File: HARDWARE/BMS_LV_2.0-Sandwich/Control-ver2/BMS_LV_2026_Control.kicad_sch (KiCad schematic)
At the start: 5 parts, among them J1 Conn_01x26

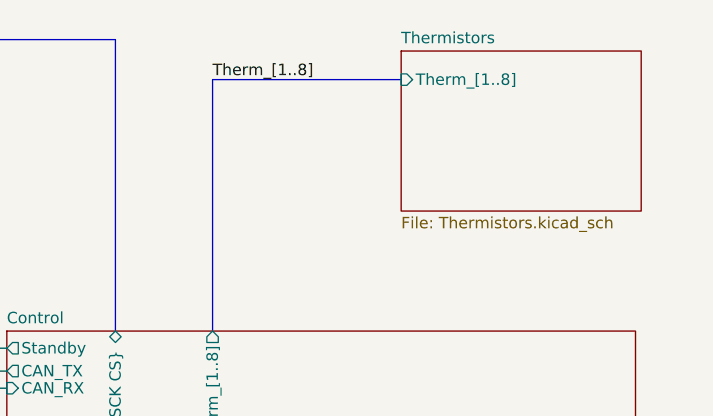
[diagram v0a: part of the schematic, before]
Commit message: Przesunięto złącze do thermistorów oraz programator aby nie bylo kolizji, przesunięto tez bezpieczniki
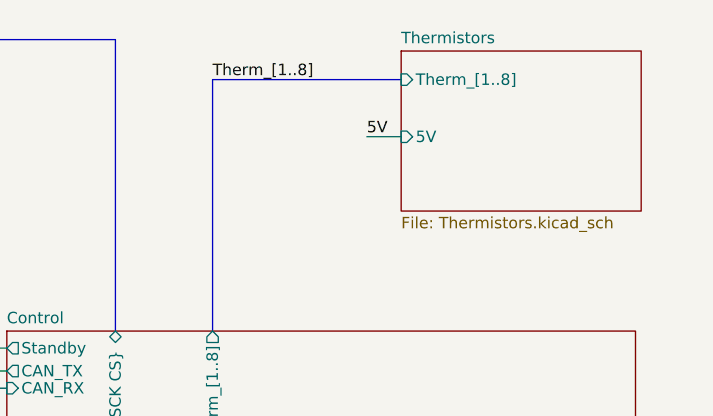
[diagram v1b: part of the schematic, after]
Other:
- sheet Thermistors ports: added 5V; removed none
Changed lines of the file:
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@@
+		)
+	)
+	(wire
+		(pts
+			(xy 173.355 62.23) (xy 177.165 62.23)
+		)
+		(stroke
+			(width 0)
+			(type default)
 		)
 	)
@@
 			)
 			(justify right bottom)
+		)
+	)
+	(label "5V"
+		(at 173.355 62.23 0)
+		(effects
+			(font
+				(size 1.27 1.27)
+			)
+			(justify left bottom)
 		)
 	)
@@
 			(effects
 				(font
+					(size 1.27 1.27)
+				)
+				(justify left)
+			)
+		)
+		(pin "5V" input
+			(at 177.165 62.23 180)
+			(effects
+				(font

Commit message: Kolejna kurwa wersja gotowa, japierdole
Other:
- sheet Control ports: added 3V3A; removed none
- sheet Power ports: added 3V3A; removed none
- sheet Thermistors ports: added 3V3A; removed 5V
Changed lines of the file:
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@@
+		(color 0 0 0 0)
+	)
+	(junction
+		(at 127.635 100.965)
+		(diameter 0)
 		(color 0 0 0 0)
 	)
@@
 	(wire
 		(pts
-			(xy 127 76.835) (xy 118.11 76.835)
+			(xy 126.365 76.835) (xy 118.11 76.835)
 		)
 		(stroke
@@
 	(wire
 		(pts
-			(xy 127 88.265) (xy 127 76.835)
+			(xy 126.365 88.265) (xy 126.365 76.835)
 		)
 		(stroke
@@
 	(wire
 		(pts
-			(xy 127 95.25) (xy 133.35 95.25)
+			(xy 125.095 95.25) (xy 133.35 95.25)
 		)
 		(stroke
@@
 	(wire
 		(pts
-			(xy 122.555 97.79) (xy 127 97.79)
+			(xy 122.555 97.79) (xy 125.095 97.79)
 		)
 		(stroke
@@
 	(wire
 		(pts
+			(xy 127.635 100.965) (xy 133.35 100.965)
+		)
+		(stroke
+			(width 0)
+			(type default)
+		)
+	)
+	(wire
+		(pts
 			(xy 57.15 95.885) (xy 34.29 95.885)
 		)
@@
 	(wire
 		(pts
+			(xy 177.165 59.69) (xy 127.635 59.69)
+		)
+		(stroke
+			(width 0)
+			(type default)
+		)
+	)
+	(wire
+		(pts
 			(xy 37.465 126.365) (xy 37.465 123.825)
 		)
@@
 	(wire
 		(pts
+			(xy 118.11 100.965) (xy 127.635 100.965)
+		)
+		(stroke
+			(width 0)
+			(type default)
+		)
+	)
+	(wire
+		(pts
 			(xy 129.54 73.66) (xy 118.11 73.66)
 		)
@@
 	(wire
 		(pts
-			(xy 133.35 88.265) (xy 127 88.265)
+			(xy 133.35 88.265) (xy 126.365 88.265)
 		)
 		(stroke
@@
 	(wire
 		(pts
+			(xy 127.635 59.69) (xy 127.635 100.965)
+		)
+		(stroke
+			(width 0)
+			(type default)
+		)
+	)
+	(wire
+		(pts
 			(xy 37.465 126.365) (xy 37.465 128.905)
 		)
@@
 	(wire
 		(pts
-			(xy 127 97.79) (xy 127 95.25)
+			(xy 125.095 97.79) (xy 125.095 95.25)
 		)
 		(stroke
@@
 		(pts
 			(xy 129.54 85.725) (xy 129.54 73.66)
-		)
-		(stroke
-			(width 0)
-			(type default)
-		)
-	)
-	(wire
-		(pts
-			(xy 173.355 62.23) (xy 177.165 62.23)
 		)
 		(stroke
@@
 		)
 	)
-	(label "5V"
-		(at 173.355 62.23 0)
-		(effects
-			(font
-				(size 1.27 1.27)
-			)
-			(justify left bottom)
-		)
-	)
 	(label "3V3"
 		(at 42.545 118.745 180)
@@
 	(label "CAN-"
 		(at 76.2 82.55 0)
+		(effects
+			(font
+				(size 1.27 1.27)
+			)
+			(justify left bottom)
+		)
+	)
+	(label "3V3A"
+		(at 121.285 100.965 0)
 		(effects
 			(font
@@
 			)
 		)
-		(pin "5V" input
-			(at 177.165 62.23 180)
+		(pin "3V3A" input
+			(at 177.165 59.69 180)
 			(effects
 				(font
@@
 			)
 		)
+		(pin "3V3A" output
+			(at 118.11 100.965 0)
+			(effects
+				(font
+					(size 1.27 1.27)
+				)
+				(justify right)
+			)
+		)
 		(instances
 			(project "BMS_LV_2026_Control"
@@
 			(effects
 				(font
+					(size 1.27 1.27)
+				)
+				(justify left)
+			)
+		)
+		(pin "3V3A" input
+			(at 133.35 100.965 180)
+			(effects
+				(font
